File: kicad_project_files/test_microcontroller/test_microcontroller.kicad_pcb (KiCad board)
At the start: 2 copper layers, 100 x 100 mm, 39 parts, among them J1 USB_C_Receptacle_USB2.0, SW1 SW_Push, SW2 SW_Push, SW3 SW_Push, SW4 SW_Push, SW5 SW_Push, SW6 SW_Push, SW7 SW_Push, SW8 SW_Push, SW9 SW_Push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

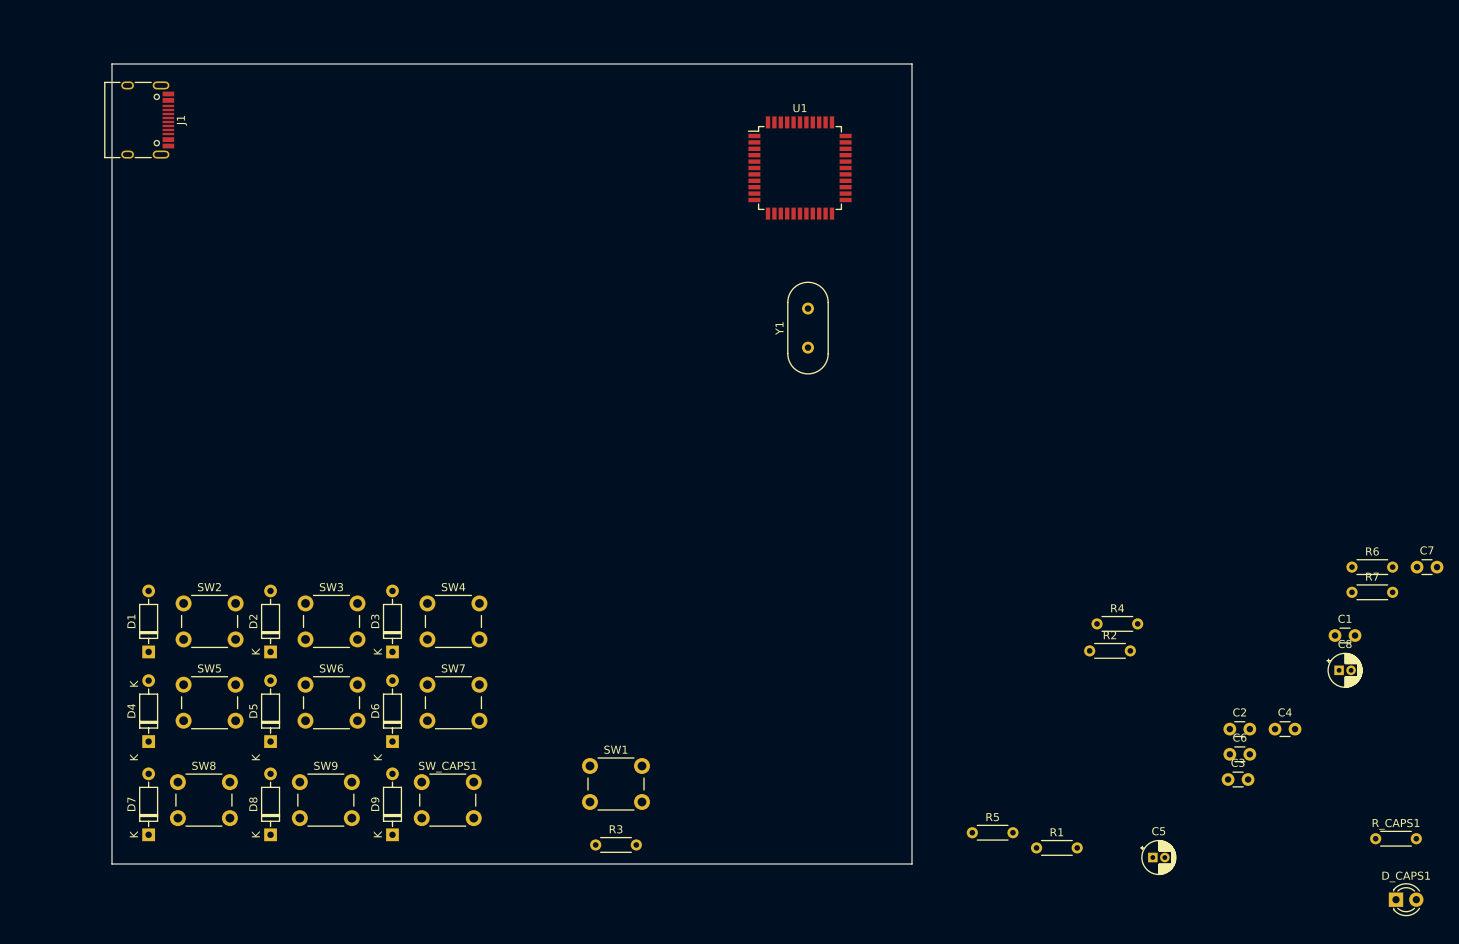
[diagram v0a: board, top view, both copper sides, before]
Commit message: add traces to pcb
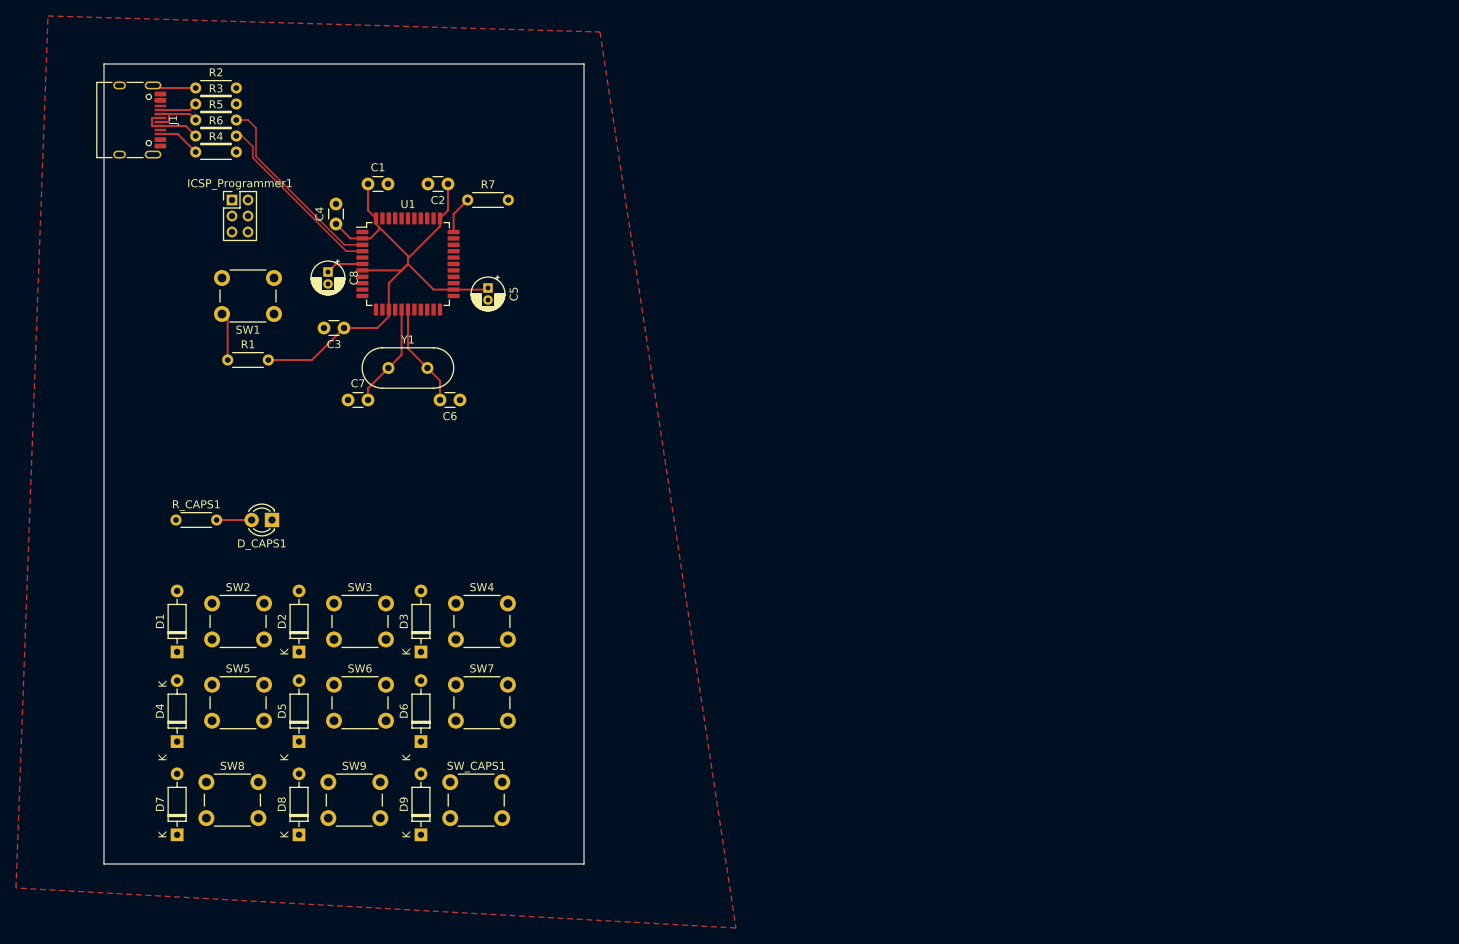
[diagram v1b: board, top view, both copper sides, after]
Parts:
- added ICSP_Programmer1: Conn_02x03_Odd_Even, Connector_PinHeader_2.00mm:PinHeader_2x03_P2.00mm_Vertical, F.Cu at (45.0, 37.0)
- moved R_CAPS1 155.2 mm to (38.0, 77.0)
- moved R6 154.3 mm to (40.5, 29.0)
- moved D_CAPS1 148.3 mm to (50.0, 77.0), turned to 180 degrees
- moved C8 135.8 mm to (57.0, 46.0), turned to -90 degrees
- moved C7 135.3 mm to (59.5, 62.0)
- moved C1 133.4 mm to (62.0, 35.0)
- moved C4 133.3 mm to (58.0, 40.0), turned to 90 degrees
- moved R2 132.1 mm to (40.5, 23.0)
- moved R5 131.8 mm to (40.5, 27.0)
- moved R4 127.2 mm to (40.5, 31.0)
- moved C3 124.1 mm to (59.0, 53.0), turned to 180 degrees
- moved R7 120.9 mm to (74.5, 37.0)
- moved C2 119.1 mm to (72.0, 35.0), turned to 180 degrees
- moved R1 118.1 mm to (44.5, 57.0)
- moved C5 109.4 mm to (77.0, 48.0), turned to -90 degrees
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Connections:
- C1 pad 1: GNDREF -> VCC
- C2 pad 1: GNDREF -> VCC
- C3 pad 1: GNDREF -> VCC
- C4 pad 1: GNDREF -> VCC
- C5 pad 1: GNDREF -> VCC
- J1 pad A4: GNDREF -> VCC
- J1 pad A9: GNDREF -> VCC
- J1 pad B4: GNDREF -> VCC
- J1 pad B9: GNDREF -> VCC
- R1 pad 2: GNDREF -> VCC
- U1 pad 10: unconnected-(U1-Pad10) -> MOSI
- U1 pad 11: unconnected-(U1-Pad11) -> MISO
- U1 pad 14: GNDREF -> VCC
- U1 pad 2: GNDREF -> VCC
- U1 pad 24: GNDREF -> VCC
- U1 pad 31: unconnected-(U1-Pad31) -> CAPS
- U1 pad 34: GNDREF -> VCC
- U1 pad 44: GNDREF -> VCC
- U1 pad 7: GNDREF -> VCC
- U1 pad 8: CAPS -> unconnected-(U1-Pad8)
- U1 pad 9: unconnected-(U1-Pad9) -> SCLK
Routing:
- net VCC: track 0.00 -> 73.4 mm
- net D-: track 0.00 -> 24.3 mm
- net D+: track 0.00 -> 22.5 mm
- net Net-(C7-Pad2): track 0.00 -> 13.0 mm
- net Net-(C6-Pad2): track 0.00 -> 13.0 mm
- net Net-(J1-PadA6): track 0.00 -> 8.00 mm
- net Net-(J1-PadA7): track 0.00 -> 7.79 mm
- net RESET: track 0.00 -> 6.04 mm
- net Net-(J1-PadS1): track 0.00 -> 5.46 mm
- net Net-(J1-PadB5): track 0.00 -> 5.35 mm
- net Net-(R7-Pad1): track 0.00 -> 4.73 mm
- net Net-(J1-PadA5): track 0.00 -> 4.73 mm
- net Net-(C8-Pad1): track 0.00 -> 4.71 mm
- net Net-(D_CAPS1-Pad2): track 0.00 -> 4.38 mm
- net Net-(D6-Pad2): track 0.00 -> 0.72 mm
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- added copper zone on F.Cu, net GNDREF
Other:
- board size 100 x 100 mm -> 60 x 100 mm

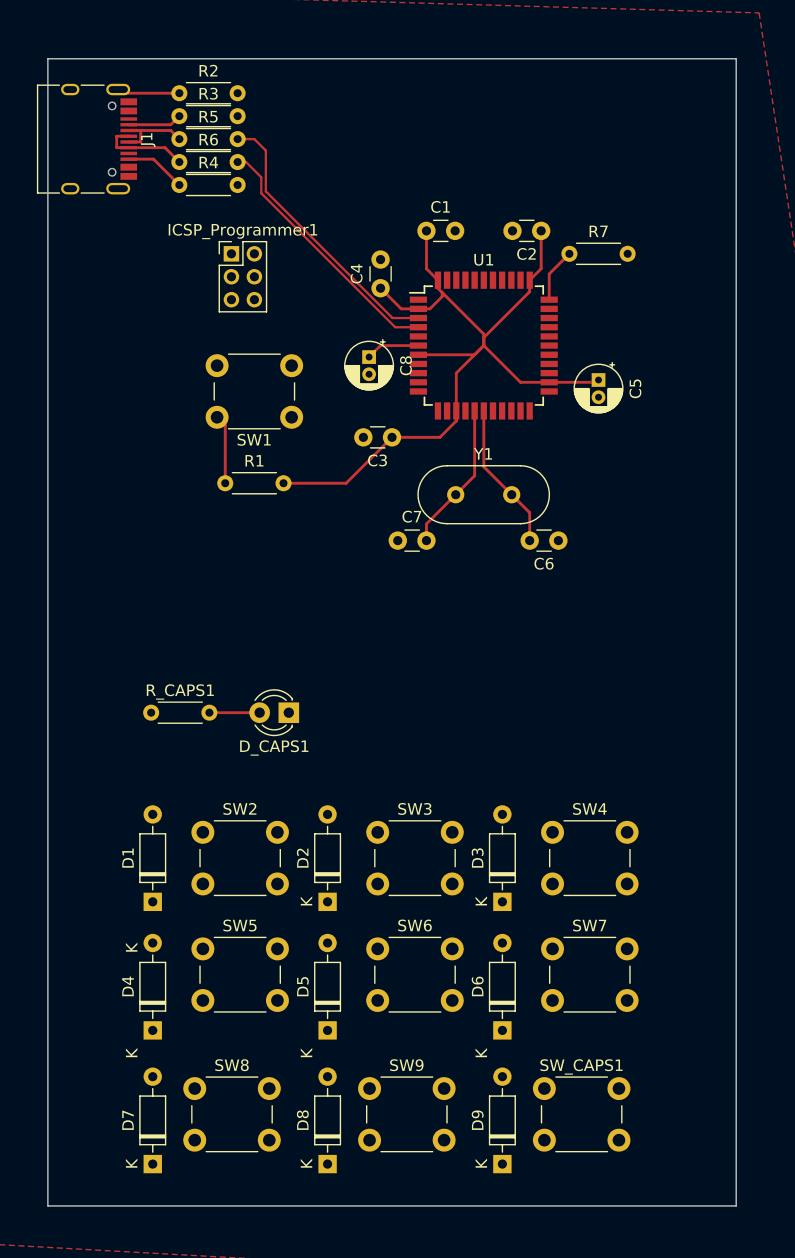
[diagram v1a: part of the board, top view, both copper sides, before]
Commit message: add pcb traces
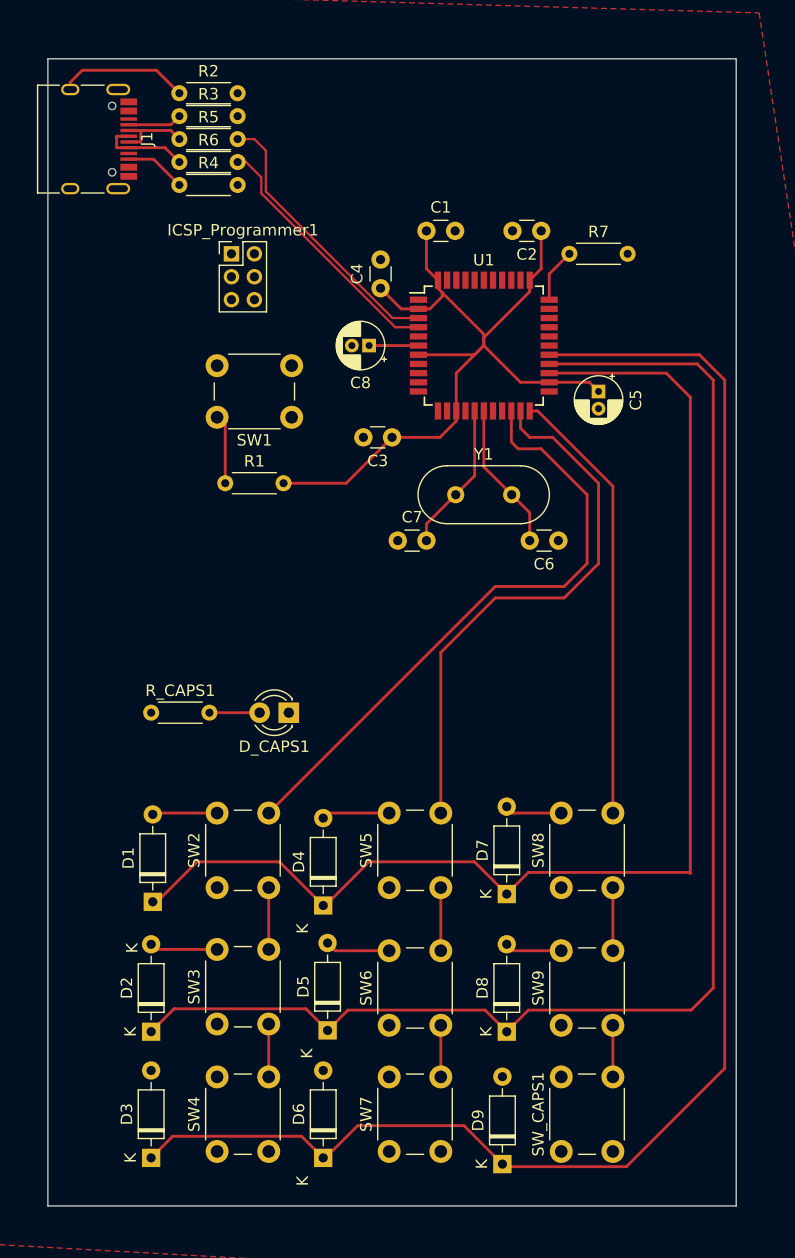
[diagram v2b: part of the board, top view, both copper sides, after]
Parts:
- moved SW4 40.4 mm to (43.8, 115.2), turned to 90 degrees
- moved D7 38.8 mm to (69.0, 92.8)
- moved D3 37.9 mm to (38.0, 115.8)
- moved SW8 36.4 mm to (73.8, 92.2), turned to 90 degrees
- moved SW7 22.7 mm to (58.8, 115.2), turned to 90 degrees
- moved SW3 21.8 mm to (43.8, 104.1), turned to 90 degrees
- moved D8 19.4 mm to (69.0, 104.8)
- moved D6 19.2 mm to (53.0, 115.8)
- moved D2 19.1 mm to (38.0, 104.8)
- moved D4 18.4 mm to (53.0, 93.8)
- moved SW9 17.6 mm to (73.8, 104.2), turned to 90 degrees
- moved SW5 17.1 mm to (58.8, 92.2), turned to 90 degrees
- moved SW6 6.73 mm to (58.8, 104.2), turned to 90 degrees
- moved SW_CAPS1 5.68 mm to (73.8, 115.2), turned to 90 degrees
- moved SW2 4.98 mm to (43.8, 92.2), turned to 90 degrees
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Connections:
- U1 pad 21: ROW1 -> COL2
- U1 pad 22: ROW2 -> COL3
- U1 pad 25: COL2 -> ROW1
- U1 pad 26: COL3 -> ROW2
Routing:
- net ROW3: track 0.00 -> 134.0 mm
- net ROW2: track 0.00 -> 121.6 mm
- net ROW1: track 0.00 -> 108.1 mm
- net COL1: track 0.00 -> 64.0 mm
- net COL2: track 0.00 -> 58.2 mm
- net COL3: track 0.00 -> 48.5 mm
- net Net-(J1-PadS1): track 5.46 -> 11.9 mm
- net Net-(D2-Pad2): track 0.00 -> 5.94 mm
- net Net-(D1-Pad2): track 0.00 -> 5.66 mm
- net Net-(D5-Pad2): track 0.00 -> 5.65 mm
- net Net-(D4-Pad2): track 0.72 -> 5.93 mm
- net Net-(D8-Pad2): track 0.00 -> 4.98 mm
- net Net-(D7-Pad2): track 0.00 -> 4.98 mm
- net Net-(D6-Pad2): track 0.72 -> 0.00 mm

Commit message: complete traces
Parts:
- moved SW1 10.4 mm to (40.8, 47.0), turned to -90 degrees
- moved ICSP_Programmer1 10.2 mm to (47.0, 47.0), turned to 180 degrees
- moved R1 3.61 mm to (41.5, 59.0)
- moved C8 1.41 mm to (56.0, 44.0)
- moved C3 1.00 mm to (59.0, 54.0), turned to -90 degrees
- moved C5 1.00 mm to (77.0, 50.0)
- moved J1 1.00 mm to (33.0, 27.0)
- moved R2 1.00 mm to (41.5, 23.0)
- moved R3 1.00 mm to (41.5, 25.0)
- moved R4 1.00 mm to (41.5, 31.0)
- moved R5 1.00 mm to (41.5, 27.0)
- moved R6 1.00 mm to (41.5, 29.0)
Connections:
- ICSP_Programmer1 pad 2: VCC -> GNDREF
- ICSP_Programmer1 pad 3: SCLK -> MOSI
- ICSP_Programmer1 pad 4: MOSI -> RESET
- ICSP_Programmer1 pad 5: RESET -> SCLK
- ICSP_Programmer1 pad 6: GNDREF -> VCC
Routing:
- net CAPS: track 0.00 -> 180.4 mm
- net VCC: track 73.6 -> 139.6 mm
- net RESET: track 6.04 -> 37.4 mm
- net SCLK: track 0.00 -> 16.1 mm
- net MOSI: track 0.00 -> 15.6 mm
- net MISO: track 0.00 -> 15.1 mm
- net COL1: track 64.0 -> 72.8 mm
- net ROW2: track 121.6 -> 113.4 mm
- net ROW1: track 108.1 -> 100.1 mm
- net ROW3: track 134.0 -> 127.4 mm
- net Net-(C8-Pad1): track 4.30 -> 5.71 mm
- net D+: track 22.5 -> 21.8 mm
- net COL2: track 58.2 -> 58.8 mm

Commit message: finish pcb and export
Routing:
- net Net-(D6-Pad2): track 0.00 -> 5.98 mm
- net Net-(D3-Pad2): track 0.00 -> 5.98 mm
- net Net-(D9-Pad2): track 0.00 -> 5.14 mm
- net VCC: track 139.6 -> 138.5 mm
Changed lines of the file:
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@@
     (pad_to_mask_clearance 0)
     (pcbplotparams
-      (layerselection 0x00010fc_ffffffff)
+      (layerselection 0x00010a8_7fffffff)
       (disableapertmacros false)
       (usegerberextensions false)
@@
       (outputformat 1)
       (mirror false)
-      (drillshape 1)
+      (drillshape 0)
       (scaleselection 1)
-      (outputdirectory "")
+      (outputdirectory "export_files/")
     )
   )
@@
     (property "Sheetname" "")
     (attr through_hole)
-    (fp_text reference "Y1" (at 2.44 -3.525) (layer "F.SilkS")
+    (fp_text reference "Y1" (at 0.45 -3.525) (layer "F.SilkS")
       (effects (font (size 1 1) (thickness 0.15)))
     )
@@
     (property "Sheetname" "")
     (attr through_hole)
-    (fp_text reference "ICSP_Programmer1" (at 1 -2.06) (layer "F.SilkS")
+    (fp_text reference "ICSP_Programmer1" (at -6 -3) (layer "F.SilkS")
       (effects (font (size 1 1) (thickness 0.15)))
     )
@@
     (property "Sheetname" "")
     (attr through_hole)
-    (fp_text reference "C3" (at 1.25 -2.05 -270) (layer "F.SilkS")
+    (fp_text reference "C3" (at 5 2 -180) (layer "F.SilkS")
       (effects (font (size 1 1) (thickness 0.15)))
     )
@@
     (property "Sheetname" "")
     (attr through_hole)
-    (fp_text reference "C7" (at 1.25 -2.05) (layer "F.SilkS")
+    (fp_text reference "C7" (at -2.5 0) (layer "F.SilkS")
       (effects (font (size 1 1) (thickness 0.15)))
     )
@@
   (segment (start 78.8 45.8) (end 72.7 45.8) (width 0.25) (layer "F.Cu") (net 9))
   (segment (start 53.19 115.81) (end 56 113) (width 0.25) (layer "F.Cu") (net 9))
+  (segment (start 38.56 108.75) (end 38 108.19) (width 0.25) (layer "F.Cu") (net 10))
+  (segment (start 43.75 108.75) (end 38.56 108.75) (width 0.25) (layer "F.Cu") (net 10))
   (segment (start 58.75 85.75) (end 53.44 85.75) (width 0.25) (layer "F.Cu") (net 11))
   (segment (start 53.44 85.75) (end 53 86.19) (width 0.25) (layer "F.Cu") (net 11))
   (segment (start 58.75 97.75) (end 54.051128 97.75) (width 0.25) (layer "F.Cu") (net 12))
   (segment (start 54.051128 97.75) (end 53.38 97.078872) (width 0.25) (layer "F.Cu") (net 12))
+  (segment (start 53.56 108.75) (end 53 108.19) (width 0.25) (layer "F.Cu") (net 13))
+  (segment (start 58.75 108.75) (end 53.56 108.75) (width 0.25) (layer "F.Cu") (net 13))
   (segment (start 69.56 85.75) (end 69 85.19) (width 0.25) (layer "F.Cu") (net 14))
   (segment (start 73.75 85.75) (end 69.56 85.75) (width 0.25) (layer "F.Cu") (net 14))
   (segment (start 73.75 97.75) (end 69.56 97.75) (width 0.25) (layer "F.Cu") (net 15))
   (segment (start 69.56 97.75) (end 69 97.19) (width 0.25) (layer "F.Cu") (net 15))
+  (segment (start 68.64 108.75) (end 68.62 108.73) (width 0.25) (layer "F.Cu") (net 16))
+  (segment (start 73.75 108.75) (end 68.64 108.75) (width 0.25) (layer "F.Cu") (net 16))
   (segment (start 47.46 77) (end 43.08 77) (width 0.25) (layer "F.Cu") (net 17))
   (segment (start 41.46 25) (end 40.71 25.75) (width 0.25) (layer "F.Cu") (net 18))
@@
   (segment (start 41.46 31) (end 39.21 28.75) (width 0.25) (layer "F.Cu") (net 22))
   (segment (start 39.21 28.75) (end 38 28.75) (width 0.25) (layer "F.Cu") (net 22))
+  (segment (start 39.46 21) (end 39 21) (width 0.25) (layer "F.Cu") (net 24))
+  (segment (start 39 21) (end 33 21) (width 0.25) (layer "F.Cu") (net 24))
+  (segment (start 41.46 23) (end 39.46 21) (width 0.25) (layer "F.Cu") (net 24))
+  (segment (start 31.95 22.05) (end 31.95 22.68) (width 0.25) (layer "F.Cu") (net 24))
   (segment (start 33 21) (end 31.95 22.05) (width 0.25) (layer "F.Cu") (net 24))
-  (segment (start 41.46 23) (end 39.46 21) (width 0.25) (layer "F.Cu") (net 24))
-  (segment (start 36.45 23) (end 36.13 22.68) (width 0.25) (layer "F.Cu") (net 24))
-  (segment (start 39 21) (end 33 21) (width 0.25) (layer "F.Cu") (net 24))
-  (segment (start 31.95 22.05) (end 31.95 22.68) (width 0.25) (layer "F.Cu") (net 24))
-  (segment (start 39.46 21) (end 39 21) (width 0.25) (layer "F.Cu") (net 24))
   (segment (start 40.75 47) (end 42.75 45) (width 0.25) (layer "F.Cu") (net 25))
+  (segment (start 63.374022 52) (end 45.75 52) (width 0.25) (layer "F.Cu") (net 25))
+  (segment (start 63.8 50.7) (end 63.8 51.574022) (width 0.25) (layer "F.Cu") (net 25))
   (segment (start 45.75 52) (end 40.75 47) (width 0.25) (layer "F.Cu") (net 25))
-  (segment (start 63.5 52) (end 45.75 52) (width 0.25) (layer "F.Cu") (net 25))
-  (segment (start 63.8 50.7) (end 63.8 51.7) (width 0.25) (layer "F.Cu") (net 25))
-  (segment (start 40.75 53.25) (end 40.75 58.29) (width 0.25) (layer "F.Cu") (net 25))
+  (segment (start 63.8 51.574022) (end 63.374022 52) (width 0.25) (layer "F.Cu") (net 25))
   (segment (start 42.75 45) (end 45 45) (width 0.25) (layer "F.Cu") (net 25))
   (segment (start 40.75 58.29) (end 41.46 59) (width 0.25) (layer "F.Cu") (net 25))
-  (segment (start 63.8 51.7) (end 63.5 52) (width 0.25) (layer "F.Cu") (net 25))
+  (segment (start 40.75 53.5) (end 40.75 58.29) (width 0.25) (layer "F.Cu") (net 25))
   (segment (start 48 27) (end 46.54 27) (width 0.2) (layer "F.Cu") (net 26))
   (segment (start 52 35.554944) (end 52 34.295006) (width 0.2) (layer "F.Cu") (net 26))
@@
   (segment (start 87 46) (end 83.6 42.6) (width 0.25) (layer "F.Cu") (net 29))
   (segment (start 48.25 104.138872) (end 48.25 108.75) (width 0.25) (layer "F.Cu") (net 30))
-  (segment (start 76 77) (end 76 58) (width 0.25) (layer "F.Cu") (net 30))
+  (segment (start 76 58) (end 72 54) (width 0.25) (layer "F.Cu") (net 30))
+  (segment (start 48.25 83.75) (end 51 81) (width 0.25) (layer "F.Cu") (net 30))
+  (segment (start 72 81) (end 76 77) (width 0.25) (layer "F.Cu") (net 30))
+  (segment (start 48.25 92.25) (end 48.25 97.638872) (width 0.25) (layer "F.Cu") (net 30))
   (segment (start 70 54) (end 69.4 53.4) (width 0.25) (layer "F.Cu") (net 30))
-  (segment (start 76 58) (end 72 54) (width 0.25) (layer "F.Cu") (net 30))
-  (segment (start 72 54) (end 70 54) (width 0.25) (layer "F.Cu") (net 30))
-  (segment (start 48.25 83.75) (end 51 81) (width 0.25) (layer "F.Cu") (net 30))
-  (segment (start 48.25 92.25) (end 48.25 97.638872) (width 0.25) (layer "F.Cu") (net 30))
   (segment (start 69.4 53.4) (end 69.4 50.7) (width 0.25) (layer "F.Cu") (net 30))
-  (segment (start 72 81) (end 76 77) (width 0.25) (layer "F.Cu") (net 30))
   (segment (start 48.25 85.75) (end 48.25 83.75) (width 0.25) (layer "F.Cu") (net 30))
   (segment (start 51 81) (end 72 81) (width 0.25) (layer "F.Cu") (net 30))
+  (segment (start 76 77) (end 76 58) (width 0.25) (layer "F.Cu") (net 30))
+  (segment (start 72 54) (end 70 54) (width 0.25) (layer "F.Cu") (net 30))
   (segment (start 70.2 52.2) (end 71 53) (width 0.25) (layer "F.Cu") (net 31))
   (segment (start 73 53) (end 77 57) (width 0.25) (layer "F.Cu") (net 31))
@@
   (segment (start 64.6 50.7) (end 64.6 47.4) (width 0.25) (layer "F.Cu") (net 52))
   (segment (start 45 38.182141) (end 45 36) (width 0.25) (layer "F.Cu") (net 52))
-  (segment (start 66.2 45.8) (end 67 45) (width 0.25) (layer "F.Cu") (net 52))
   (segment (start 37.045 29.45) (end 36.220978 29.45) (width 0.25) (layer "F.Cu") (net 52))
   (segment (start 48.818348 42.000489) (end 45 38.182141) (width 0.25) (layer "F.Cu") (net 52))
